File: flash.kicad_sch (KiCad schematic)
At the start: 1 part, among them U2 IS25LP064A-JLLE

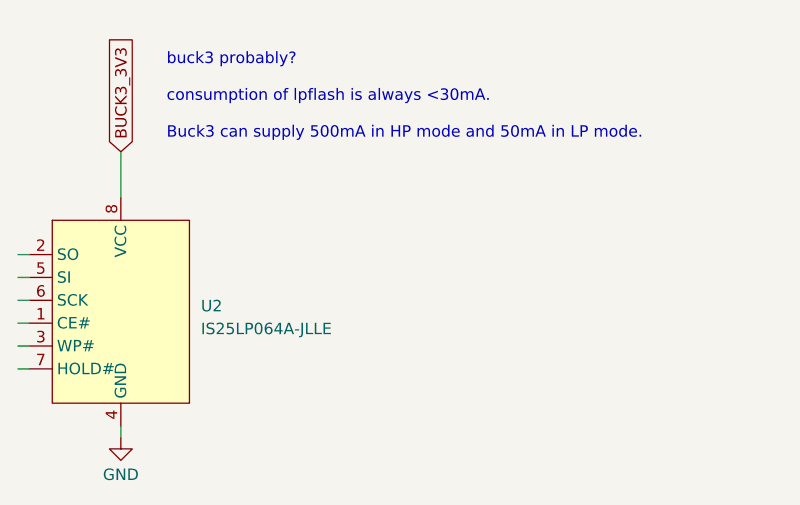
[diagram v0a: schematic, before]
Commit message: added QSMP1570 symbol and footprint to project. Modified Symbol. Cleaning of schematic.
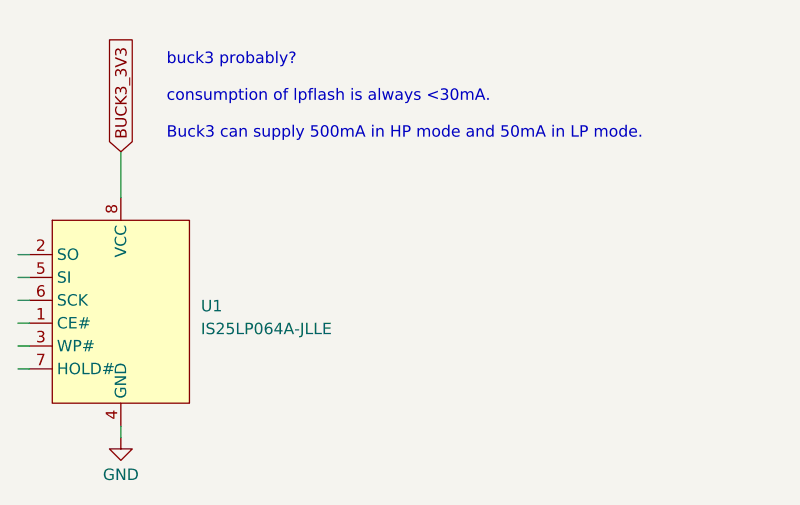
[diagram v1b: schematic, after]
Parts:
- renumbered U2 to U1
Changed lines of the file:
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@@
   (symbol (lib_id "ARMband:IS25LP064A-JLLE") (at 64.77 54.61 0) (unit 1)
     (in_bom yes) (on_board yes) (dnp no) (fields_autoplaced)
-    (property "Reference" "U2" (at 73.66 55.245 0)
+    (property "Reference" "U1" (at 73.66 55.245 0)
       (effects (font (size 1.27 1.27)) (justify left))
     )
@@
     (instances
       (project "armband"
-        (path "/017c50c6-333c-4d31-ad5a-278994a09b14/486c2044-10e8-4af1-b5d5-a133bea25b9d"
-          (reference "U2") (unit 1)
+        (path "/017c50c6-333c-4d31-ad5a-278994a09b14/4f745a0b-8724-4289-9dd5-c25d5562a5b2/5f118be0-d1f5-46b1-b05a-c3ccf67cbeb8"
+          (reference "U1") (unit 1)
         )
       )
@@
           (reference "#PWR065") (unit 1)
         )
-        (path "/017c50c6-333c-4d31-ad5a-278994a09b14/486c2044-10e8-4af1-b5d5-a133bea25b9d"
-          (reference "#PWR075") (unit 1)
+        (path "/017c50c6-333c-4d31-ad5a-278994a09b14/4f745a0b-8724-4289-9dd5-c25d5562a5b2/5f118be0-d1f5-46b1-b05a-c3ccf67cbeb8"
+          (reference "#PWR01") (unit 1)
         )
       )
